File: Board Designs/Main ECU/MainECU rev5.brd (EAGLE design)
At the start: 120.6 x 78.9 mm, 164 parts, among them Q10 MMBT3904LT3G, Q11 MMBT3904LT3G, Q9 MMBT3904LT3G, X1 CONNECTOR-37, X2 CONNECTOR-4AUTOSPORT, X3 CONNECTOR-4NANO-FIT-VERTICAL-4, X4 CONNECTOR-4NANO-FIT-VERTICAL-4

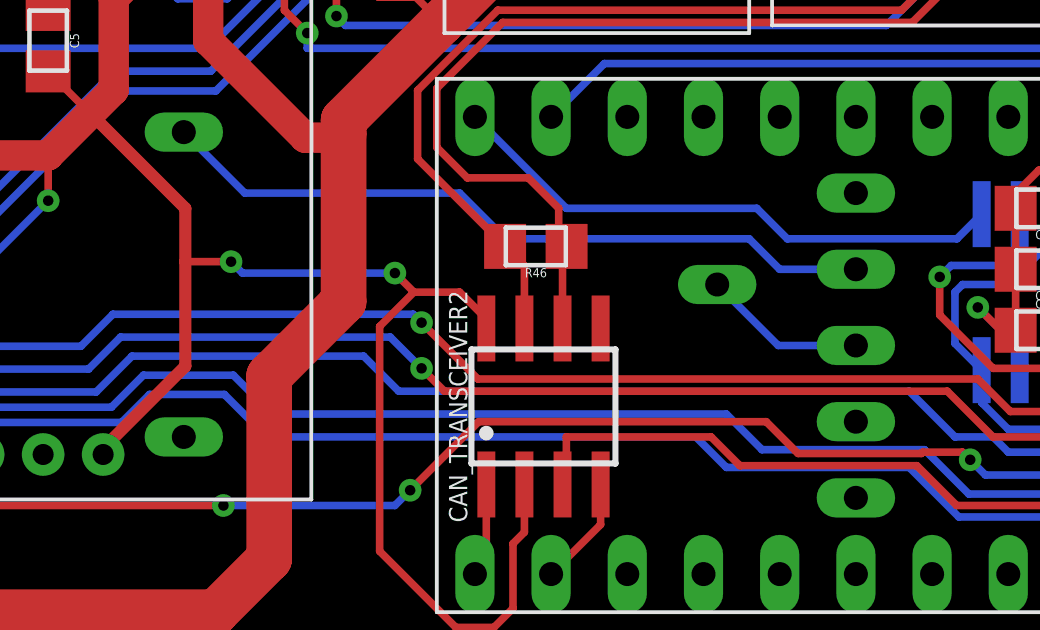
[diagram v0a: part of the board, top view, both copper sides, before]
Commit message: Corrected VBAT connection for RTC coin cell
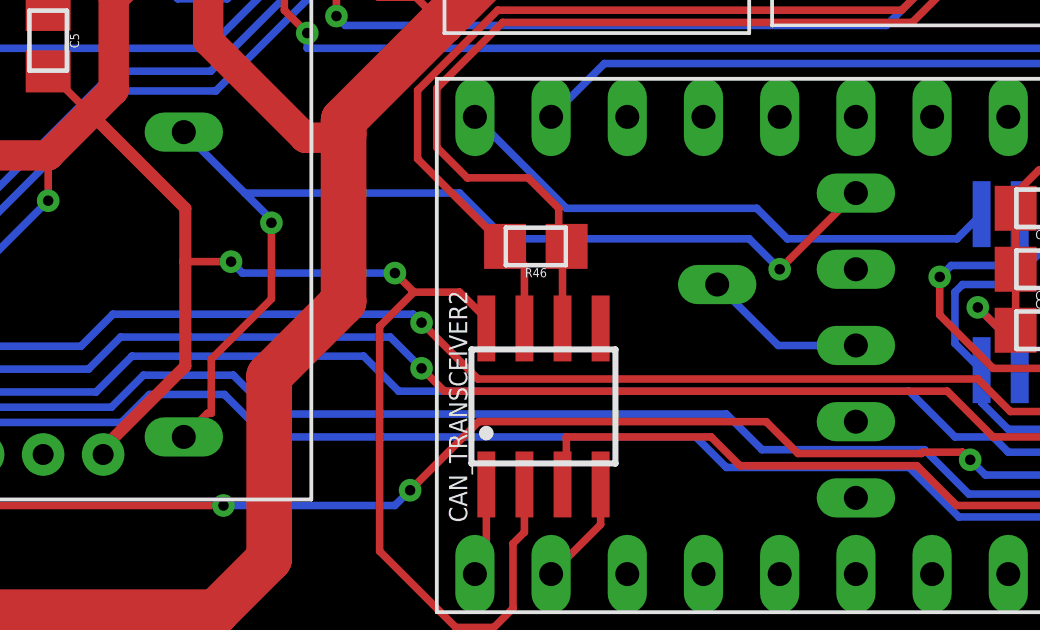
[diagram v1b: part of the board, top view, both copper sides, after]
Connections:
- net N$60: now also U$2.VBAT; no longer U$2.3.3V_2
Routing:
- net N$60: track 24.3 -> 35.1 mm, vias 0 -> 2
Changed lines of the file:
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@@
 <?xml version="1.0" encoding="utf-8"?>
 <!DOCTYPE eagle SYSTEM "eagle.dtd">
-<eagle version="9.2.2">
+<eagle version="8.6.0">
 <drawing>
 <settings>
@@
 <param name="checkStop" value="0"/>
 <param name="checkValues" value="0"/>
-<param name="checkNames" value="1"/>
-<param name="checkWireStubs" value="1"/>
-<param name="checkPolygonWidth" value="0"/>
 <param name="useDiameter" value="13"/>
 <param name="maxErrors" value="50"/>
@@
 <contactref element="U$16" pad="+_0"/>
 <contactref element="U$16" pad="+_1"/>
-<contactref element="U$2" pad="3.3V_2"/>
-<wire x1="72.39" y1="13.208" x2="69.85" y2="13.208" width="0.254" layer="16"/>
 <wire x1="69.85" y1="13.208" x2="68.834" y2="14.224" width="0.254" layer="16"/>
 <wire x1="68.834" y1="14.224" x2="60.706" y2="14.224" width="0.254" layer="16"/>
@@
 <wire x1="49.9872" y1="17.78" x2="52.0192" y2="15.748" width="0.254" layer="16"/>
 <wire x1="52.0192" y1="15.748" x2="59.182" y2="15.748" width="0.254" layer="16"/>
-<wire x1="49.9872" y1="7.62" x2="52.0192" y2="15.748" width="0" layer="19" extent="16-16"/>
+<contactref element="U$2" pad="VBAT"/>
+<via x="69.85" y="13.208" extent="1-16" drill="0.35"/>
+<wire x1="69.85" y1="13.208" x2="72.39" y2="15.748" width="0.254" layer="1"/>
+<wire x1="52.0192" y1="15.748" x2="52.9082" y2="14.859" width="0.254" layer="16"/>
+<wire x1="52.9082" y1="14.859" x2="52.9082" y2="14.7574" width="0.254" layer="16"/>
+<via x="52.9082" y="14.7574" extent="1-16" drill="0.35"/>
+<wire x1="52.9082" y1="14.7574" x2="52.9082" y2="12.2174" width="0.254" layer="1"/>
+<wire x1="50.9016" y1="10.2108" x2="50.9016" y2="8.4074" width="0.254" layer="1"/>
+<wire x1="52.9082" y1="12.2174" x2="50.9016" y2="10.2108" width="0.254" layer="1"/>
+<wire x1="50.9016" y1="8.4074" x2="50.7746" y2="8.4074" width="0.254" layer="1"/>
+<wire x1="50.7746" y1="8.4074" x2="49.9872" y2="7.62" width="0.254" layer="1"/>
 </signal>
 <signal name="N$61">
@@
 </signal>
 </signals>
-<mfgpreviewcolors>
-<mfgpreviewcolor name="soldermaskcolor" color="0xC8008000"/>
-<mfgpreviewcolor name="silkscreencolor" color="0xFFFEFEFE"/>
-<mfgpreviewcolor name="backgroundcolor" color="0xFF282828"/>
-<mfgpreviewcolor name="coppercolor" color="0xFFFFBF00"/>
-<mfgpreviewcolor name="substratecolor" color="0xFF786E46"/>
-</mfgpreviewcolors>
 <errors>
 </errors>

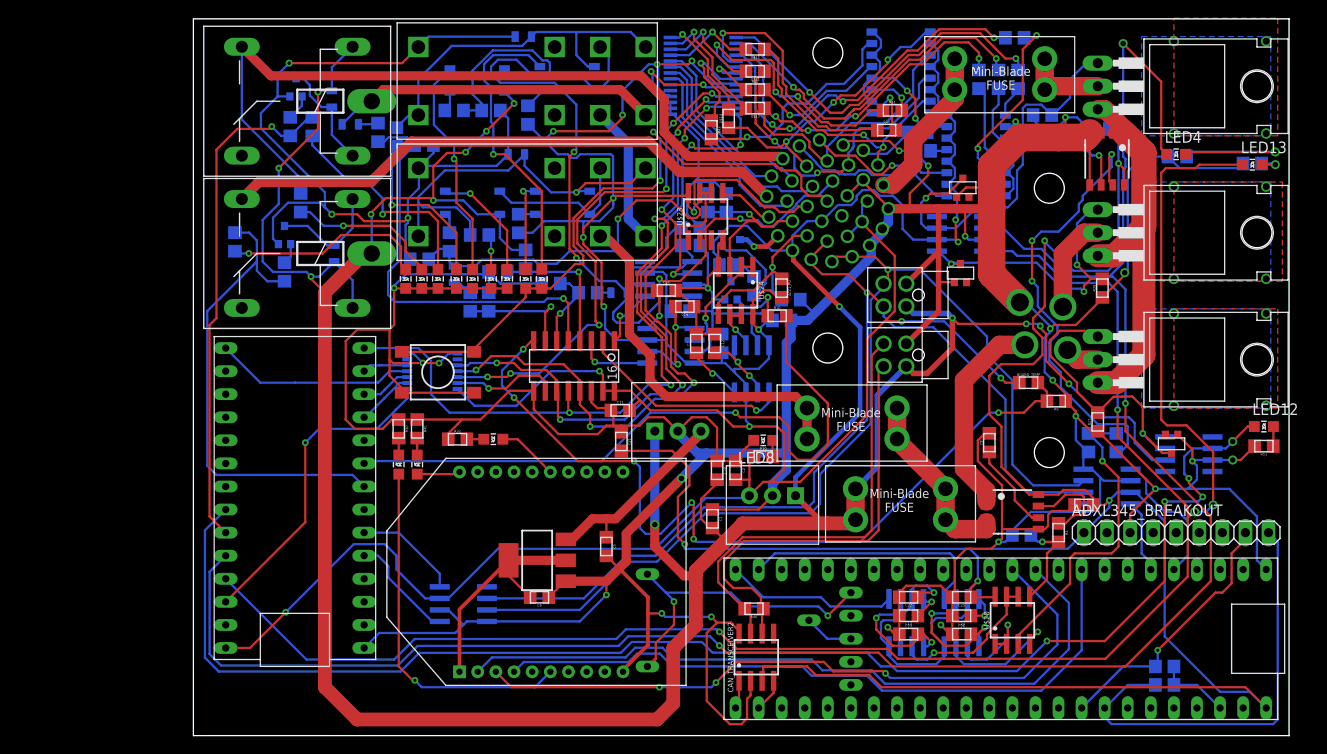
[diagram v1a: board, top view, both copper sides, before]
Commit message: Main ECU rev5: Widen cooling traces, Move thermistor closer to cooling switching components
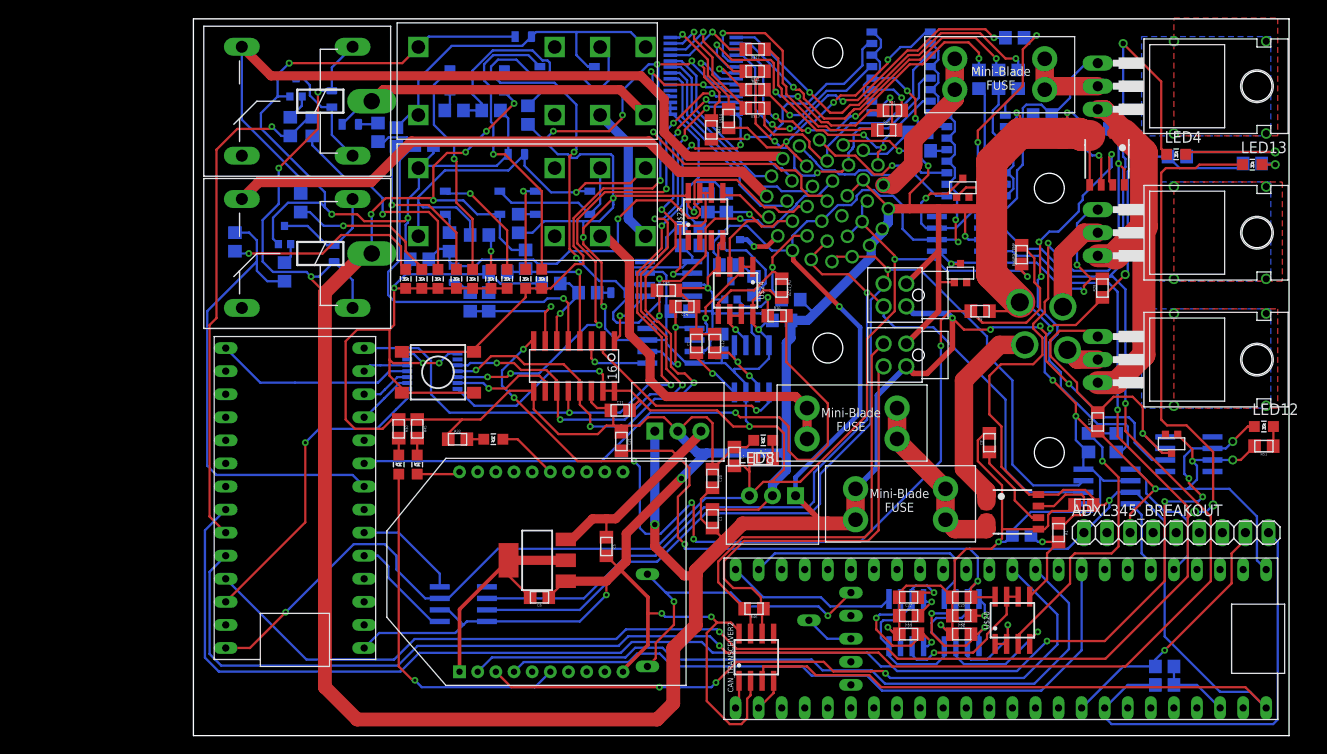
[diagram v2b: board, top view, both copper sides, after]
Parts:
- moved BOARD_TEMP 14.1 mm to (91.2, 53.0), turned to 90 degrees
- moved R9 13.0 mm to (86.6, 46.7)
- moved C2 1.53 mm to (59.6, 30.7)
- moved C20 1.02 mm to (57.1, 28.3)
- moved R20 0.25 mm to (62.7, 30.5)
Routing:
- net TEMPSENSE: track 91.5 -> 110.5 mm
- net GND: track 844.9 -> 852.2 mm
- net N$6: track 48.9 -> 48.0 mm
- net +12V: track 417.5 -> 416.7 mm
- net TELEMETRY5V: track 299.5 -> 299.0 mm
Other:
- board text added: "HyTech 2019 Main ECU rev5"
- board text added: "Updates by Nathan Cheek, Soohyun Kim"
- board text removed: "HyTech 2019 Main ECU rev4"
- board text removed: "Updates by Nathan Cheek"

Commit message: Main ECU rev{1-4}: Add warning about RTC cell assembly, specify current sensor input capacitor value, lower XBee LED resistor to 33R; Main ECU rev{2,4}: Specify MCP3208 input capacitor value; Main ECU rev4: Lower relay-controlling transistors' base resistor to 1k; Main ECU rev5: make all relevant changes previously listed
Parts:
- C10, C9: value (none) -> 0.1uF
- C11: value (none) -> 1uF
- R45: value 2.3k -> 33
- R47, R50: value 2.2k -> 1k
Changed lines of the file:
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@@
 <attribute name="VALUE" x="56.4388" y="23.876" size="0.3048" layer="27" rot="R270" align="top-center"/>
 </element>
-<element name="C10" library="HyTechDevices" package="0805" value="" x="99.822" y="66.802" smashed="yes" rot="MR0">
+<element name="C10" library="HyTechDevices" package="0805" value="0.1uF" x="99.822" y="66.802" smashed="yes" rot="MR0">
 <attribute name="NAME" x="99.822" y="67.5259" size="0.3048" layer="26" rot="MR0" align="bottom-center" display="off"/>
 <attribute name="VALUE" x="99.822" y="66.0908" size="0.3048" layer="28" rot="MR0" align="top-center"/>
@@
 <attribute name="VALUE" x="88.3412" y="32.258" size="0.3048" layer="27" rot="R90" align="top-center"/>
 </element>
-<element name="C9" library="HyTechDevices" package="0805" value="" x="98.044" y="25.4" smashed="yes" rot="R180">
+<element name="C9" library="HyTechDevices" package="0805" value="0.1uF" x="98.044" y="25.4" smashed="yes" rot="R180">
 <attribute name="NAME" x="98.044" y="24.6761" size="0.3048" layer="25" rot="R180" align="bottom-center"/>
 <attribute name="VALUE" x="98.044" y="26.1112" size="0.3048" layer="27" rot="R180" align="top-center"/>
@@
 <attribute name="VALUE" x="79.756" y="65.7098" size="0.3048" layer="28" rot="MR0" align="top-center"/>
 </element>
-<element name="R45" library="HyTechDevices" package="0805" value="2.3k" x="24.638" y="33.782" smashed="yes" rot="R270">
+<element name="R45" library="HyTechDevices" package="0805" value="33" x="24.638" y="33.782" smashed="yes" rot="R270">
 <attribute name="NAME" x="25.3619" y="33.782" size="0.3048" layer="25" rot="R270" align="bottom-center"/>
 <attribute name="VALUE" x="23.9268" y="33.782" size="0.3048" layer="27" rot="R270" align="top-center"/>
@@
 <attribute name="VALUE" x="46.4058" y="32.385" size="0.3048" layer="27" rot="R270" align="top-center"/>
 </element>
-<element name="C11" library="HyTechDevices" package="0805" value="" x="46.99" y="35.814" smashed="yes">
+<element name="C11" library="HyTechDevices" package="0805" value="1uF" x="46.99" y="35.814" smashed="yes">
 <attribute name="NAME" x="46.99" y="36.5379" size="0.3048" layer="25" align="bottom-center"/>
 <attribute name="VALUE" x="46.99" y="35.1028" size="0.3048" layer="27" align="top-center"/>
@@
 </element>
 <element name="Q9" library="HyTechDevices" package="SOT23" value="MMBT3904LT3G" x="10.033" y="55.118" smashed="yes" rot="MR0"/>
-<element name="R47" library="HyTechDevices" package="0805" value="2.2k" x="10.033" y="51.054" smashed="yes" rot="MR90">
+<element name="R47" library="HyTechDevices" package="0805" value="1k" x="10.033" y="51.054" smashed="yes" rot="MR90">
 <attribute name="NAME" x="10.7569" y="51.054" size="0.3048" layer="26" rot="MR90" align="bottom-center"/>
 <attribute name="VALUE" x="9.3218" y="51.054" size="0.3048" layer="28" rot="MR90" align="top-center"/>
 </element>
 <element name="Q11" library="HyTechDevices" package="SOT23" value="MMBT3904LT3G" x="11.303" y="71.374" smashed="yes" rot="MR0"/>
-<element name="R50" library="HyTechDevices" package="0805" value="2.2k" x="10.668" y="67.056" smashed="yes" rot="MR90">
+<element name="R50" library="HyTechDevices" package="0805" value="1k" x="10.668" y="67.056" smashed="yes" rot="MR90">
 <attribute name="NAME" x="11.3919" y="67.056" size="0.3048" layer="26" rot="MR90" align="bottom-center"/>
 <attribute name="VALUE" x="9.9568" y="67.056" size="0.3048" layer="28" rot="MR90" align="top-center"/>
